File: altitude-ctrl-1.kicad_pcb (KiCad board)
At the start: 2 copper layers, 90 x 90 mm, 93 parts, among them J1 Conn_01x02, J10 Conn_01x02, J11 Conn_01x04, J2 Conn_01x02, J3 Conn_01x05, J4 TC2030, J5 Conn_01x04_Pin, J6 Conn_01x02, J7 Conn_01x05, J8 Conn_01x05, J9 Conn_01x02, SW1 SW_Push, SW2 SW_SPST, SW3 SW_Push, SW4 SW_SPST, SW5 SW_Push, U1 HT753-1, U2 ULN2003A, U3 LM73100, U4 LM73100, U5 MAX6675, U6 STM32F103C8Tx, U7 SN65HVD230, Y1 8M

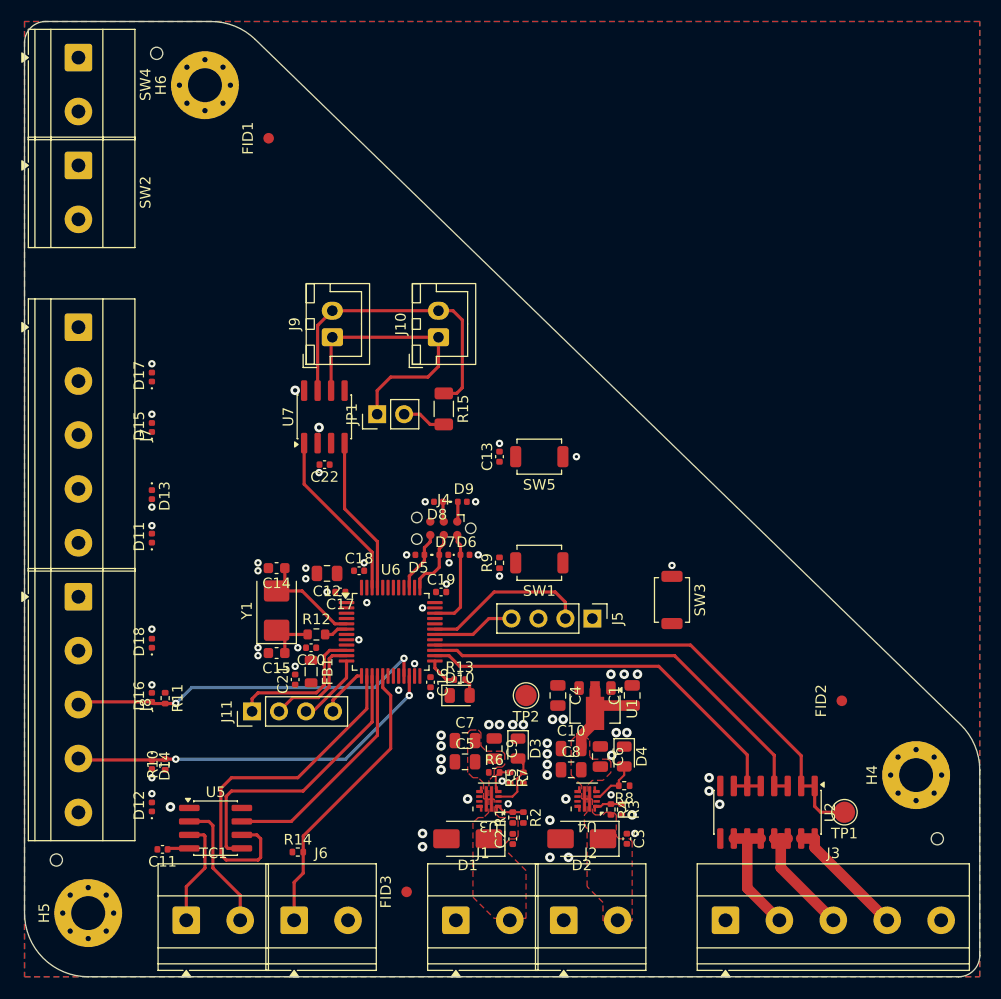
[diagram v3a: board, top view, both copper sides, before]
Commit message: pcb: add steper, lms & bau routing
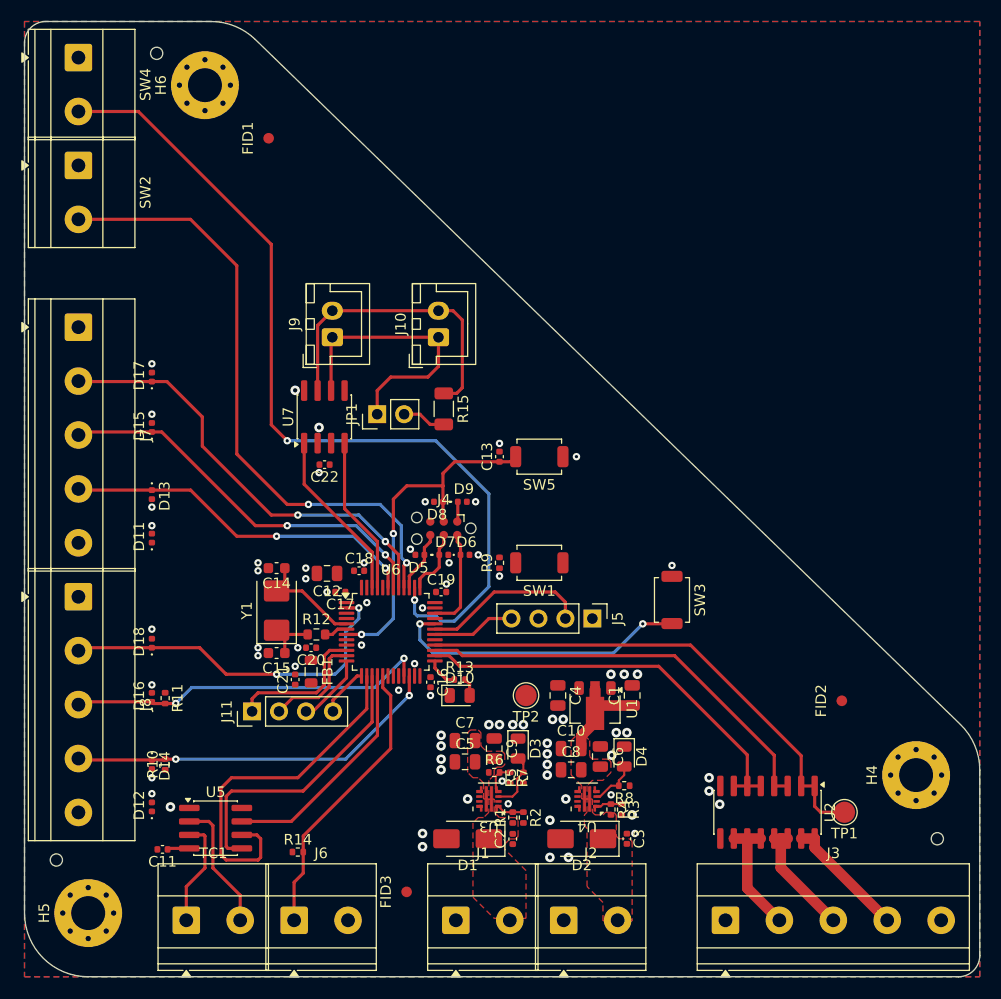
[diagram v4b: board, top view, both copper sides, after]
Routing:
- net /BAU: track 0.00 -> 83.4 mm, vias 0 -> 2
- net /LMS: track 0.00 -> 58.9 mm, vias 0 -> 2
- net /EN: track 0.00 -> 41.6 mm, vias 0 -> 2
- net /DIR: track 0.00 -> 37.2 mm, vias 0 -> 2
- net /STEP: track 0.00 -> 34.0 mm, vias 0 -> 2
- net /RST: track 0.00 -> 33.7 mm, vias 0 -> 2
- net /NRST: track 1.90 -> 33.6 mm, vias 0 -> 2
- net /BTN1: track 0.00 -> 28.3 mm, vias 0 -> 2

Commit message: pcb: add misc power routing
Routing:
- net +5V: track 10.9 -> 142.4 mm, vias 0 -> 2
- net +12V: track 0.00 -> 94.6 mm

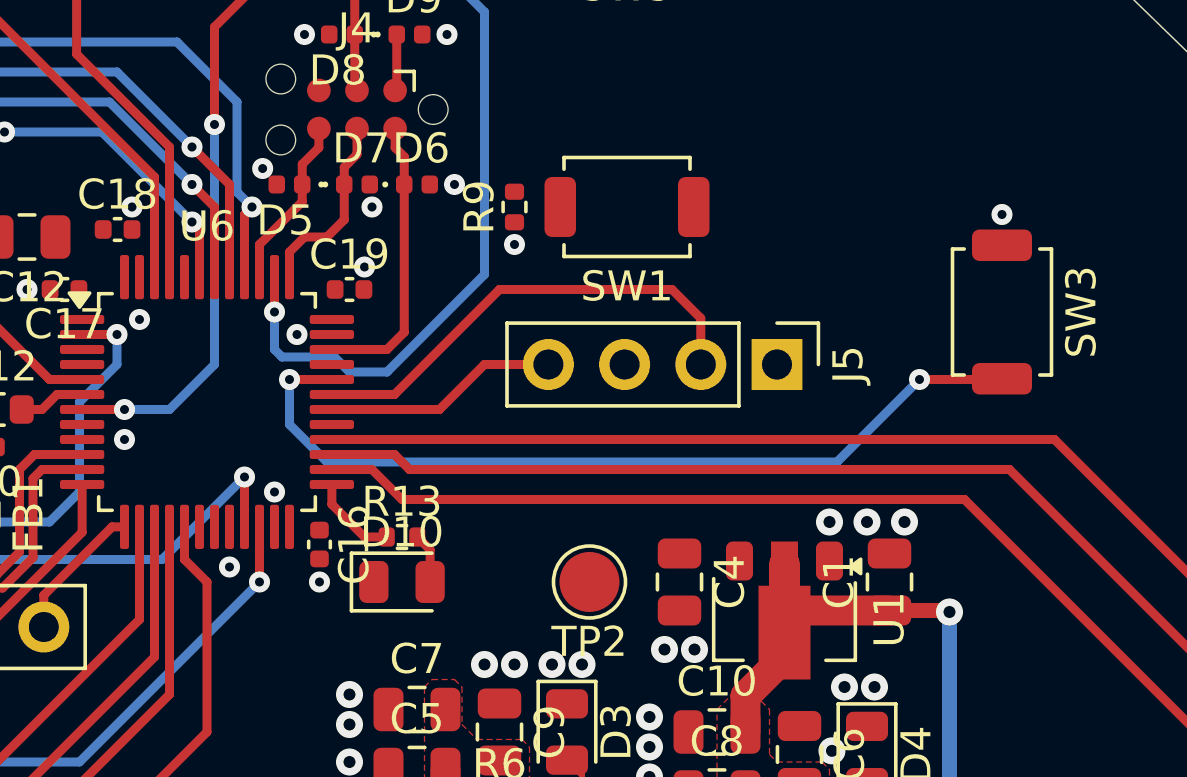
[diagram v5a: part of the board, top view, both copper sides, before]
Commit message: pcb: add boot routing
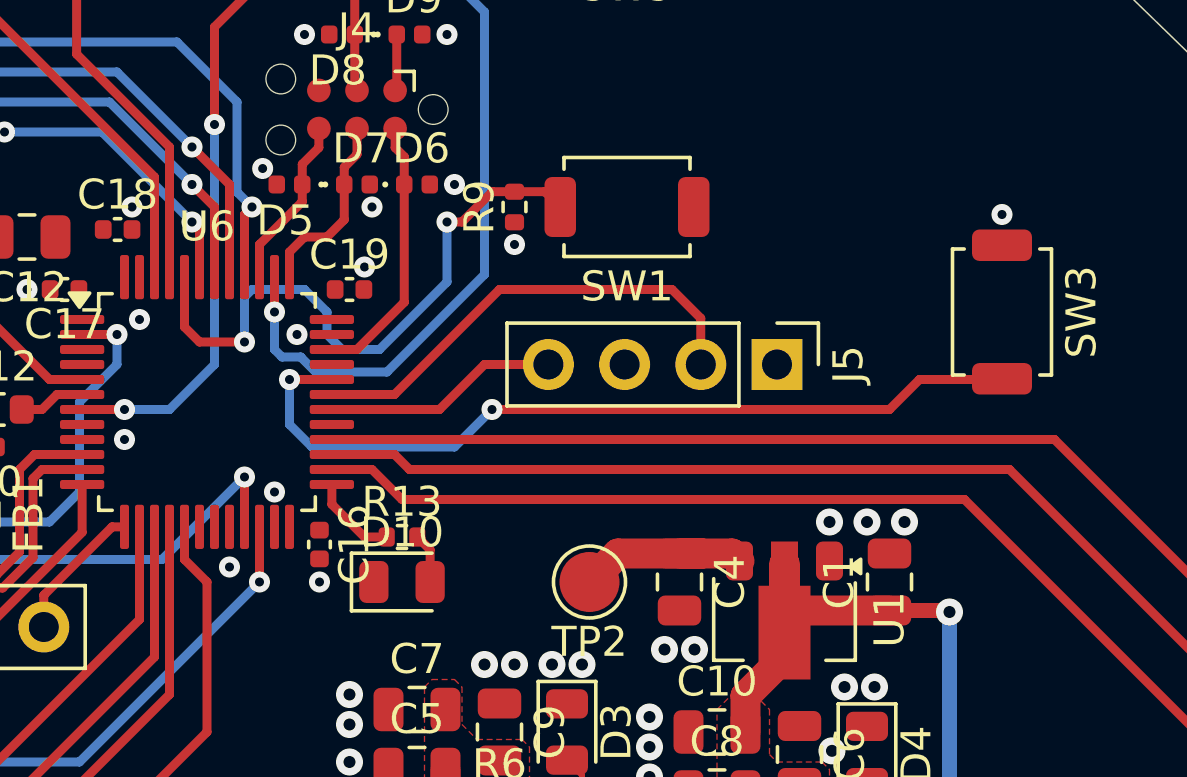
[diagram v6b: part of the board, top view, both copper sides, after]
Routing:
- net /BOOT: track 0.00 -> 20.8 mm, vias 0 -> 2
- net +3V3: track 3.97 -> 10.2 mm
- net /SWDIO: track 9.57 -> 8.98 mm
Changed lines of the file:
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@@
+	)
+	(segment
+		(start 180.25 91.55)
+		(end 181 91.55)
+		(width 1)
+		(layer "F.Cu")
+		(net "+3V3")
+	)
+	(segment
+		(start 181 91.55)
+		(end 182 91.55)
+		(width 1)
+		(layer "F.Cu")
+		(net "+3V3")
 	)
 	(segment
@@
 	)
 	(segment
+		(start 178.2 91.55)
+		(end 177.25 92.5)
+		(width 1)
+		(layer "F.Cu")
+		(net "+3V3")
+	)
+	(segment
 		(start 170.825 76.06)
 		(end 170.77 76.115)
@@
 	)
 	(segment
+		(start 182 91.55)
+		(end 182.25 91.8)
+		(width 1)
+		(layer "F.Cu")
+		(net "+3V3")
+	)
+	(segment
 		(start 145.525 106.905)
 		(end 143.575 106.905)
@@
 	)
 	(segment
+		(start 181 91.55)
+		(end 178.2 91.55)
+		(width 1)
+		(layer "F.Cu")
+		(net "+3V3")
+	)
+	(segment
 		(start 170.77 78.02)
 		(end 171.075 78.325)
@@
 	)
 	(segment
-		(start 170.5 84.75)
-		(end 171.075 84.175)
+		(start 169.5 84.75)
+		(end 171.075 83.175)
 		(width 0.3)
 		(layer "F.Cu")
@@
 	)
 	(segment
-		(start 171.075 84.175)
+		(start 168.6625 84.75)
+		(end 169.5 84.75)
+		(width 0.3)
+		(layer "F.Cu")
+		(net "/SWDIO")
+	)
+	(segment
+		(start 171.075 83.175)
 		(end 171.075 79.25)
-		(width 0.3)
-		(layer "F.Cu")
-		(net "/SWDIO")
-	)
-	(segment
-		(start 168.6625 84.75)
-		(end 170.5 84.75)
 		(width 0.3)
 		(layer "F.Cu")
@@
 	)
 	(segment
+		(start 187.25 86.75)
+		(end 174 86.75)
+		(width 0.3)
+		(layer "F.Cu")
+		(net "/BTN1")
+	)
+	(segment
+		(start 190.975 85.75)
+		(end 188.25 85.75)
+		(width 0.3)
+		(layer "F.Cu")
+		(net "/BTN1")
+	)
+	(segment
 		(start 188.25 85.75)
-		(end 190.975 85.75)
-		(width 0.3)
-		(layer "F.Cu")
-		(net "/BTN1")
-	)
-	(segment
-		(start 190.975 85.75)
-		(end 191 85.725)
+		(end 187.25 86.75)
 		(width 0.3)
 		(layer "F.Cu")
@@
 		(net "/BTN1")
 	)
-	(via
-		(at 188.25 85.75)
+	(segment
+		(start 191 85.725)
+		(end 190.975 85.75)
+		(width 0.3)
+		(layer "F.Cu")
+		(net "/BTN1")
+	)
+	(via
+		(at 174 86.75)
 		(size 0.7)
 		(drill 0.3)
@@
 	)
 	(segment
+		(start 172.75 88)
+		(end 168 88)
+		(width 0.3)
+		(layer "B.Cu")
+		(net "/BTN1")
+	)
+	(segment
 		(start 167.25 87.25)
-		(end 168.5 88.5)
+		(end 167.25 85.75)
 		(width 0.3)
 		(layer "B.Cu")
@@
 	)
 	(segment
-		(start 167.25 85.75)
+		(start 174 86.75)
+		(end 172.75 88)
+		(width 0.3)
+		(layer "B.Cu")
+		(net "/BTN1")
+	)
+	(segment
+		(start 168 88)
 		(end 167.25 87.25)
-		(width 0.3)
-		(layer "B.Cu")
-		(net "/BTN1")
-	)
-	(segment
-		(start 168.5 88.5)
-		(end 185.5 88.5)
-		(width 0.3)
-		(layer "B.Cu")
-		(net "/BTN1")
-	)
-	(segment
-		(start 185.5 88.5)
-		(end 188.25 85.75)
 		(width 0.3)
 		(layer "B.Cu")
@@
 	)
 	(segment
+		(start 174.75 79.49)
+		(end 175.765 79.49)
+		(width 0.3)
+		(layer "F.Cu")
+		(net "/BOOT")
+	)
+	(segment
+		(start 172.5 80.5)
+		(end 173 80.5)
+		(width 0.3)
+		(layer "F.Cu")
+		(net "/BOOT")
+	)
+	(segment
+		(start 164.25 84.5)
+		(end 165.75 84.5)
+		(width 0.3)
+		(layer "F.Cu")
+		(net "/BOOT")
+	)
+	(segment
+		(start 174.01 79.49)
+		(end 174.75 79.49)
+		(width 0.3)
+		(layer "F.Cu")
+		(net "/BOOT")
+	)
+	(segment
+		(start 163.75 82.3375)
+		(end 163.75 84)
+		(width 0.3)
+		(layer "F.Cu")
+		(net "/BOOT")
+	)
+	(segment
+		(start 163.75 84)
+		(end 164.25 84.5)
+		(width 0.3)
+		(layer "F.Cu")
+		(net "/BOOT")
+	)
+	(segment
+		(start 173 80.5)
+		(end 174.01 79.49)
+		(width 0.3)
+		(layer "F.Cu")
+		(net "/BOOT")
+	)
+	(segment
+		(start 175.765 79.49)
+		(end 176.275 80)
+		(width 0.3)
+		(layer "F.Cu")
+		(net "/BOOT")
+	)
+	(via
+		(at 172.5 80.5)
+		(size 0.7)
+		(drill 0.3)
+		(layers "F.Cu" "B.Cu")
+		(net "/BOOT")
+	)
+	(via
+		(at 165.75 84.5)
+		(size 0.7)
+		(drill 0.3)
+		(layers "F.Cu" "B.Cu")
+		(net "/BOOT")
+	)
+	(segment
+		(start 168.5 84.25)
+		(end 169 84.75)
+		(width 0.3)
+		(layer "B.Cu")
+		(net "/BOOT")
+	)
+	(segment
+		(start 170.25 84.75)
+		(end 172.5 82.5)
+		(width 0.3)
+		(layer "B.Cu")
+		(net "/BOOT")
+	)
+	(segment
+		(start 167.75 82.75)
+		(end 168.5 83.5)
+		(width 0.3)
+		(layer "B.Cu")
+		(net "/BOOT")
+	)
+	(segment
+		(start 172.5 82.5)
+		(end 172.5 80.5)
+		(width 0.3)
+		(layer "B.Cu")
+		(net "/BOOT")
+	)
+	(segment
+		(start 165.75 84.5)
+		(end 165.75 83)
+		(width 0.3)
+		(layer "B.Cu")
+		(net "/BOOT")
+	)
+	(segment
+		(start 168.5 83.5)
+		(end 168.5 84.25)
+		(width 0.3)
+		(layer "B.Cu")
+		(net "/BOOT")
+	)
+	(segment
+		(start 169 84.75)
+		(end 170.25 84.75)
+		(width 0.3)
+		(layer "B.Cu")
+		(net "/BOOT")
+	)
+	(segment
+		(start 166 82.75)
+		(end 167.75 82.75)
+		(width 0.3)
+		(layer "B.Cu")
+		(net "/BOOT")
+	)
+	(segment
+		(start 165.75 83)
+		(end 166 82.75)
+		(width 0.3)
+		(layer "B.Cu")
+		(net "/BOOT")
+	)
+	(segment
 		(start 153.25 50)
 		(end 140.73 37.48)
@@
 	)
 	(segment
+		(start 166.75 83.5)
+		(end 166.75 84.75)
+		(width 0.3)
+		(layer "B.Cu")
+		(net "/BAU")
+	)
+	(segment
+		(start 166.75 84.75)
+		(end 167 85)
+		(width 0.3)
+		(layer "B.Cu")
+		(net "/BAU")
+	)
+	(segment
+		(start 173.75 82.25)
+		(end 173.75 73.5)
+		(width 0.3)
+		(layer "B.Cu")
+		(net "/BAU")
+	)
+	(segment
+		(start 168.75 68.5)
+		(end 154.75 68.5)
+		(width 0.3)
+		(layer "B.Cu")
+		(net "/BAU")
+	)
+	(segment
 		(start 170.5 85.5)
 		(end 173.75 82.25)
@@
 	)
 	(segment
-		(start 166.75 84.75)
-		(end 167 85)
-		(width 0.3)
-		(layer "B.Cu")
-		(net "/BAU")
-	)
-	(segment
 		(start 173.75 73.5)
 		(end 168.75 68.5)
@@
 	)
 	(segment
-		(start 173.75 82.25)
-		(end 173.75 73.5)
+		(start 167.625 85)
+		(end 168.125 85.5)
 		(width 0.3)
 		(layer "B.Cu")
@@
 	)
 	(segment
-		(start 168.75 85)
-		(end 169.25 85.5)
+		(start 167 85)
+		(end 167.625 85)
 		(width 0.3)
 		(layer "B.Cu")
@@
 	)
 	(segment
-		(start 166.75 83.5)
-		(end 166.75 84.75)
-		(width 0.3)
-		(layer "B.Cu")
-		(net "/BAU")
-	)
-	(segment
-		(start 169.25 85.5)
+		(start 168.125 85.5)
 		(end 170.5 85.5)
 		(width 0.3)
 		(layer "B.Cu")
-		(net "/BAU")
-	)
-	(segment
-		(start 167 85)
-		(end 168.75 85)
-		(width 0.3)
-		(layer "B.Cu")
-		(net "/BAU")
-	)
-	(segment
-		(start 168.75 68.5)
-		(end 154.75 68.5)
-		(width 0.3)
-		(layer "B.Cu")

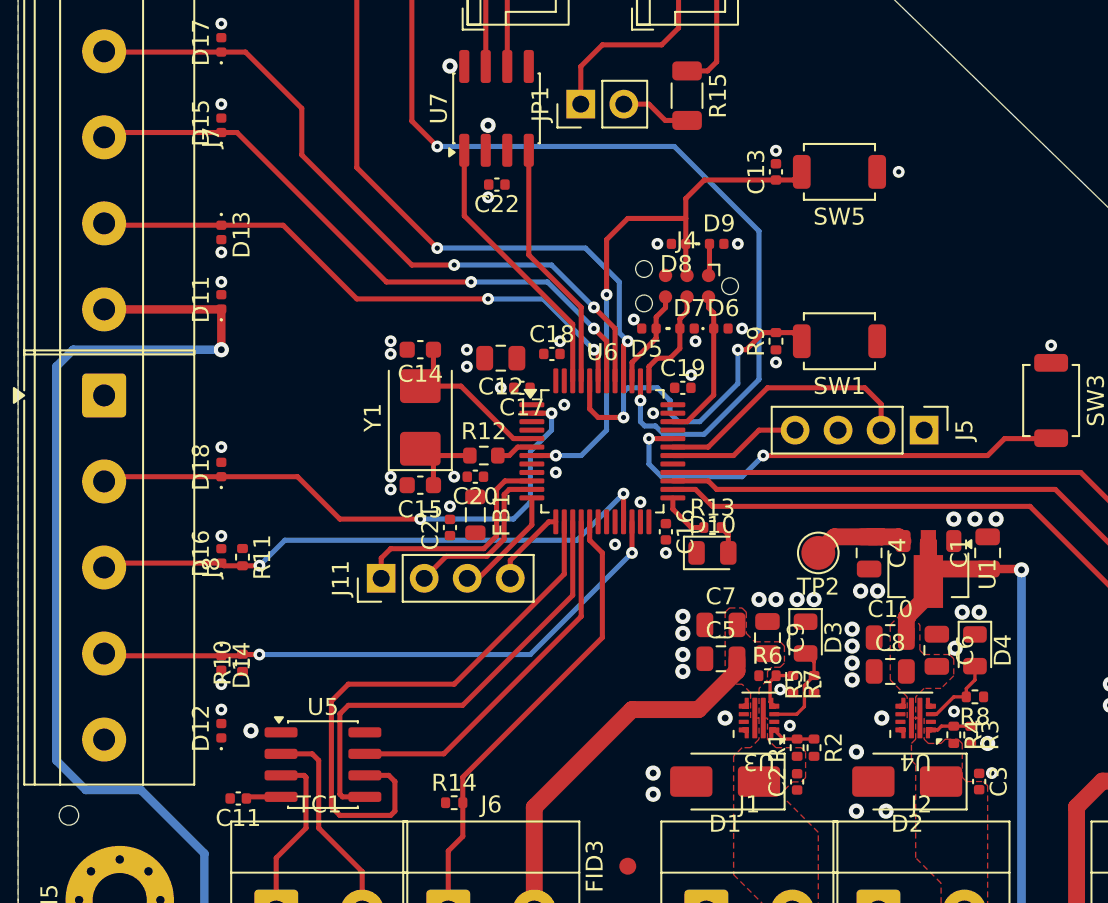
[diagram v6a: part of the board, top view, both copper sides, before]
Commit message: pcb: add +3V3 pwr routing
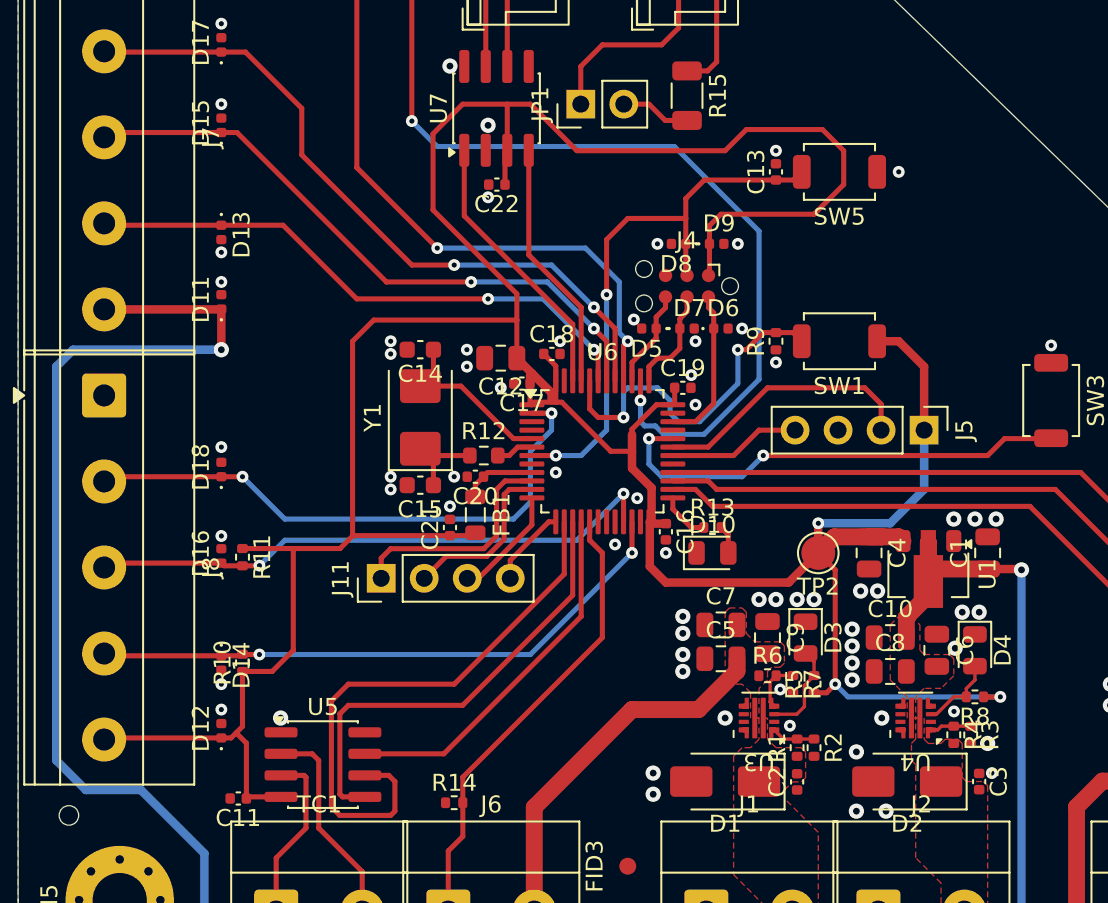
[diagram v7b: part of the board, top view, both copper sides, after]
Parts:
- moved C17 0.25 mm to (159.8, 82.5)
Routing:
- net +3V3: track 10.2 -> 211.0 mm, vias 0 -> 3
- net Net-(U6-VDDA): track 0.00 -> 4.35 mm
- net GND: vias 73 -> 72

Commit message: pcb: add missing routing
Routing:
- net GND: track 0.00 -> 4.06 mm
- net +5V: track 142.4 -> 144.9 mm
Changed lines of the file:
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@@
 		(layer "Edge.Cuts")
+	)
+	(segment
+		(start 185.16074 101.859892)
+		(end 184.640632 102.38)
+		(width 0.2)
+		(layer "F.Cu")
+		(net "GND")
+	)
+	(segment
+		(start 162.25 82.3375)
+		(end 162.25 81)
+		(width 0.3)
+		(layer "F.Cu")
+		(net "GND")
+	)
+	(segment
+		(start 162 80.75)
+		(end 162 80)
+		(width 0.3)
+		(layer "F.Cu")
+		(net "GND")
+	)
+	(segment
+		(start 162.25 81)
+		(end 162 80.75)
+		(width 0.3)
+		(layer "F.Cu")
+		(net "GND")
+	)
+	(segment
+		(start 184.640632 102.38)
+		(end 184.375025 102.38)
+		(width 0.2)
+		(layer "F.Cu")
+		(net "GND")
+	)
+	(segment
+		(start 184.280025 102.475)
+		(end 183.9 102.475)
+		(width 0.2)
+		(layer "F.Cu")
+		(net "GND")
+	)
+	(segment
+		(start 185.263144 101.859892)
+		(end 185.16074 101.859892)
+		(width 0.2)
+		(layer "F.Cu")
+		(net "GND")
+	)
+	(segment
+		(start 184.375025 102.38)
+		(end 184.280025 102.475)
+		(width 0.2)
+		(layer "F.Cu")
+		(net "GND")
 	)
 	(via
@@
 	)
 	(segment
+		(start 184.25 100)
+		(end 184.25 99.2)
+		(width 0.2)
+		(layer "F.Cu")
+		(net "+5V")
+	)
+	(segment
+		(start 183.9 100.35)
+		(end 184.25 100)
+		(width 0.2)
+		(layer "F.Cu")
+		(net "+5V")
+	)
+	(segment
 		(start 189.2 93.45)
 		(end 189.25 93.5)
@@
 		(layer "F.Cu")
 		(net "+5V")
+	)
+	(segment
+		(start 183.9 101.55)
+		(end 183.9 100.35)
+		(width 0.2)
+		(layer "F.Cu")
+		(net "+5V")
